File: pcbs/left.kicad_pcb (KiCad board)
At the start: 2 copper layers, 123.5 x 93.6 mm, 27 parts

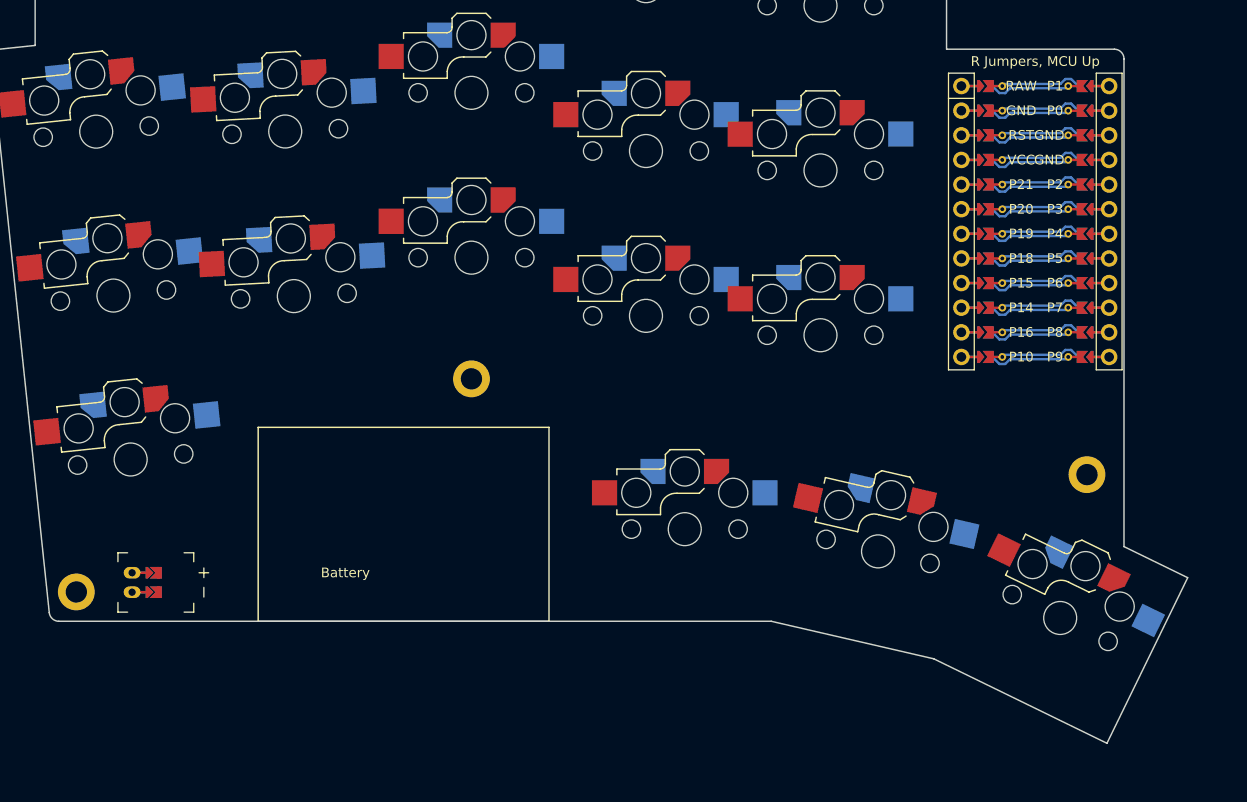
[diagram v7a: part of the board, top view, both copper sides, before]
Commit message: Cut out battery area
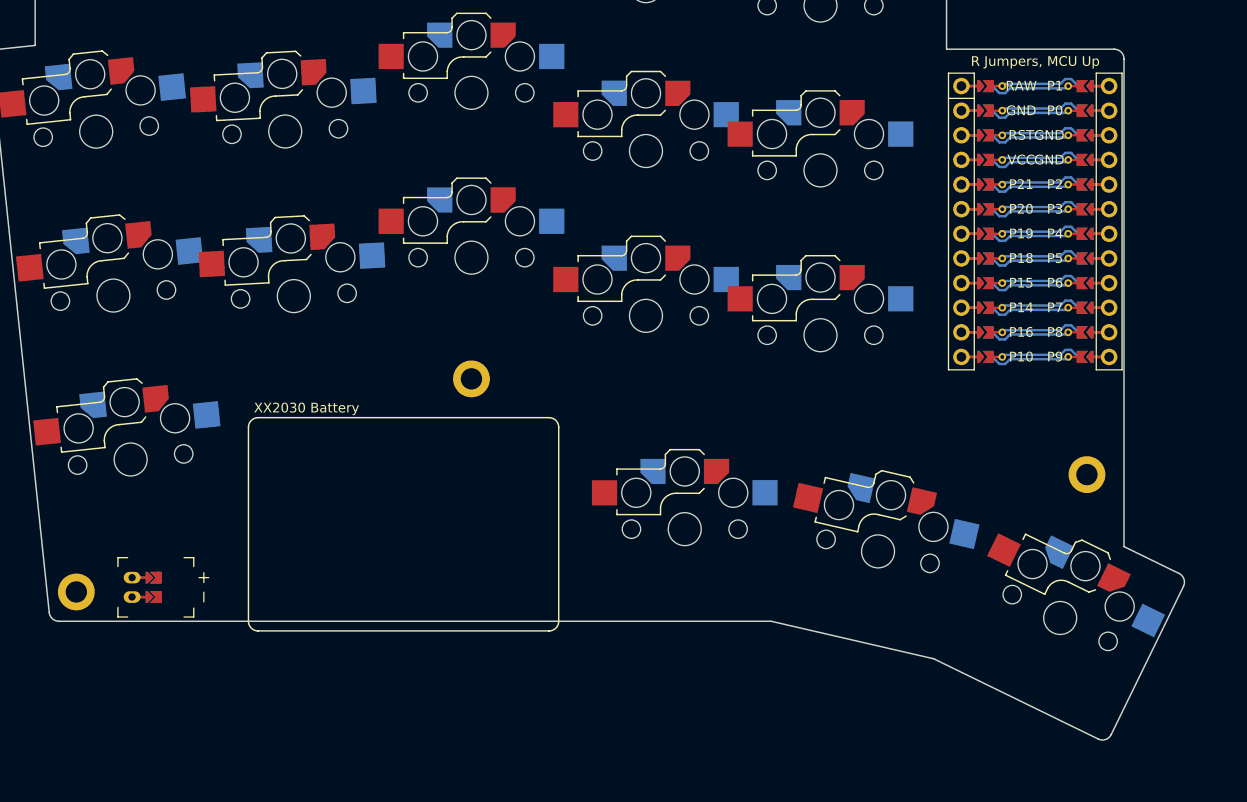
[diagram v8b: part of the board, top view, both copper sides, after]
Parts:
- moved JST1 0.50 mm to (100.1, 113.2)
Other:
- board size 123.5 x 93.6 mm -> 123.2 x 93.2 mm
- board text added: "XX2030 Battery"
- board text removed: "Battery"
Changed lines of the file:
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@@
     (footprint "ceoloide:battery_connector_jst_ph_2"
         (layer "F.Cu")
-        (at 100.1483666 112.68429119999999 90)
+        (at 100.1483666 113.18429119999999 90)
         (property "Reference" "JST1"
             (at 0 4.8 90)
@@
         )
     )
-    (segment (start 101.9483666 113.68429119999999) (end 100.1483666 113.68429119999999) (width 0.25) (layer "F.Cu") (net 53))
-    (segment (start 101.9483666 113.68429119999999) (end 100.1483666 113.68429119999999) (width 0.25) (layer "B.Cu") (net 53))
-    (segment (start 101.9483666 111.68429119999999) (end 100.1483666 111.68429119999999) (width 0.25) (layer "F.Cu") (net 54))
-    (segment (start 101.9483666 111.68429119999999) (end 100.1483666 111.68429119999999) (width 0.25) (layer "B.Cu") (net 54))
-  (gr_text "Battery"
-    (at 122.1483666 111.68429119999999 0)
+    (segment (start 101.9483666 114.18429119999999) (end 100.1483666 114.18429119999999) (width 0.25) (layer "F.Cu") (net 53))
+    (segment (start 101.9483666 114.18429119999999) (end 100.1483666 114.18429119999999) (width 0.25) (layer "B.Cu") (net 53))
+    (segment (start 101.9483666 112.18429119999999) (end 100.1483666 112.18429119999999) (width 0.25) (layer "F.Cu") (net 54))
+    (segment (start 101.9483666 112.18429119999999) (end 100.1483666 112.18429119999999) (width 0.25) (layer "B.Cu") (net 54))
+  (gr_text "XX2030 Battery"
+    (at 118.1483666 94.68429119999999 0)
     (layer "F.SilkS" )
     (effects
@@
         (thickness 0.15)
       )
+    )
+  )
+  (gr_text "XX2030 Battery"
+    (at 118.1483666 94.68429119999999 0)
+    (layer "B.SilkS" )
+    (effects
+      (font
+        (size 1 1)
+        (thickness 0.15)
+      )
+      (justify  mirror)
     )
   )
@@
     (filled_areas_thickness no)
     (fill
-      yes
+      (mode hatch)
       (thermal_gap 0.5)
       (thermal_bridge_width 0.5)
@@
       (island_removal_mode 1)
       (island_area_min 5)
+      (hatch_thickness 1)
+      (hatch_gap 1.5)
+      (hatch_orientation 0)
+      (hatch_border_algorithm hatch_thickness)
+      (hatch_min_hole_area 0.3)
     )
     (polygon
@@
 (gr_line (start 145.1483667 35.68429119999999) (end 125.1483667 35.68429119999999) (layer Edge.Cuts) (stroke (width 0.15) (type default)))
 (gr_line (start 125.1483667 35.68429119999999) (end 125.1483667 39.15278895091144) (layer Edge.Cuts) (stroke (width 0.15) (type default)))
-(gr_line (start 92.5989108808387 116.68429119999999) (end 166.06423773916333 116.68429119999999) (layer Edge.Cuts) (stroke (width 0.15) (type default)))
-(gr_line (start 166.06423773916333 116.68429119999999) (end 182.8265398929574 120.55417358778122) (layer Edge.Cuts) (stroke (width 0.15) (type default)))
-(gr_line (start 182.8265398929574 120.55417358778122) (end 200.6915044 129.2674989) (layer Edge.Cuts) (stroke (width 0.15) (type default)))
-(gr_line (start 200.6915044 129.2674989) (end 209.02055620000002 112.190412) (layer Edge.Cuts) (stroke (width 0.15) (type default)))
-(gr_line (start 209.02055620000002 112.190412) (end 202.4483666 108.9849409801272) (layer Edge.Cuts) (stroke (width 0.15) (type default)))
+(gr_line (start 92.5989108808387 116.68429119999999) (end 165.95030193237426 116.68429119999999) (layer Edge.Cuts) (stroke (width 0.15) (type default)))
+(gr_line (start 166.17525303237426 116.70992109999997) (end 182.71552494111705 120.52854376659285) (layer Edge.Cuts) (stroke (width 0.15) (type default)))
+(gr_line (start 182.92894494111707 120.60411986659285) (end 199.79271042772405 128.82912779290854) (layer Edge.Cuts) (stroke (width 0.15) (type default)))
+(gr_line (start 201.12987552772407 128.3687048929085) (end 208.58218508851954 113.08920597378722) (layer Edge.Cuts) (stroke (width 0.15) (type default)))
+(gr_line (start 208.1217621885195 111.75204087378721) (end 202.4483666 108.98494098012722) (layer Edge.Cuts) (stroke (width 0.15) (type default)))
+(gr_arc (start 166.17525303237426 116.70992109999999) (mid 166.06350513237425 116.69071929999998) (end 165.95030193237426 116.68429119999999) (layer Edge.Cuts) (stroke (width 0.15) (type default)))
+(gr_arc (start 182.92894494111707 120.60411976659283) (mid 182.82438064111705 120.56027236659284) (end 182.71552494111705 120.52854376659283) (layer Edge.Cuts) (stroke (width 0.15) (type default)))
+(gr_arc (start 199.79271042772405 128.82912789290856) (mid 200.55664972772405 128.87585239290857) (end 201.12987562772406 128.36870489290857) (layer Edge.Cuts) (stroke (width 0.15) (type default)))
+(gr_arc (start 208.58218518851953 113.08920597378723) (mid 208.62890968851954 112.32526667378723) (end 208.12176218851954 111.75204077378723) (layer Edge.Cuts) (stroke (width 0.15) (type default)))
 (gr_line (start 184.1483667 57.684291099999996) (end 201.4483666 57.684291099999996) (layer Edge.Cuts) (stroke (width 0.15) (type default)))
-(gr_line (start 202.4483666 108.9849409801272) (end 202.4483666 58.684291099999996) (layer Edge.Cuts) (stroke (width 0.15) (type default)))
+(gr_line (start 202.4483666 108.98494098012722) (end 202.4483666 58.684291099999996) (layer Edge.Cuts) (stroke (width 0.15) (type default)))
 (gr_arc (start 202.4483666 58.684291099999996) (mid 202.1554734 57.9771843) (end 201.4483666 57.684291099999996) (layer Edge.Cuts) (stroke (width 0.15) (type default)))
 (gr_arc (start 91.6043889808387 115.78881969999996) (mid 91.9297802808387 116.42743599999996) (end 92.5989108808387 116.68429119999996) (layer Edge.Cuts) (stroke (width 0.15) (type default)))
@@
 (gr_arc (start 91.1483667 39.18429119999999) (mid 90.44125989999999 39.47718439999999) (end 90.1483667 40.18429119999999) (layer Edge.Cuts) (stroke (width 0.15) (type default)))
 (gr_arc (start 184.1483667 40.18429119999999) (mid 183.8554735 39.47718439999999) (end 183.1483667 39.18429119999999) (layer Edge.Cuts) (stroke (width 0.15) (type default)))
-(gr_line (start 113.1483666 96.68429119999999) (end 113.1483666 116.68429119999999) (layer F.SilkS) (stroke (width 0.15) (type default)))
-(gr_line (start 113.1483666 116.68429119999999) (end 143.1483666 116.68429119999999) (layer F.SilkS) (stroke (width 0.15) (type default)))
-(gr_line (start 143.1483666 116.68429119999999) (end 143.1483666 96.68429119999999) (layer F.SilkS) (stroke (width 0.15) (type default)))
-(gr_line (start 143.1483666 96.68429119999999) (end 113.1483666 96.68429119999999) (layer F.SilkS) (stroke (width 0.15) (type default)))
+(gr_line (start 112.1483666 96.68429119999999) (end 112.1483666 116.68429119999999) (layer F.SilkS) (stroke (width 0.15) (type default)))
+(gr_arc (start 112.1483666 116.68429119999999) (mid 112.4412598 117.391398) (end 113.1483666 117.68429119999999) (layer F.SilkS) (stroke (width 0.15) (type default)))
+(gr_line (start 113.1483666 117.68429119999999) (end 143.1483666 117.68429119999999) (layer F.SilkS) (stroke (width 0.15) (type default)))
+(gr_arc (start 143.1483666 117.68429119999999) (mid 143.8554734 117.391398) (end 144.1483666 116.68429119999999) (layer F.SilkS) (stroke (width 0.15) (type default)))
+(gr_line (start 144.1483666 116.68429119999999) (end 144.1483666 96.68429119999999) (layer F.SilkS) (stroke (width 0.15) (type default)))
+(gr_arc (start 144.1483666 96.68429119999999) (mid 143.8554734 95.97718439999998) (end 143.1483666 95.68429119999999) (layer F.SilkS) (stroke (width 0.15) (type default)))
+(gr_line (start 143.1483666 95.68429119999999) (end 113.1483666 95.68429119999999) (layer F.SilkS) (stroke (width 0.15) (type default)))
+(gr_arc (start 113.1483666 95.68429119999999) (mid 112.4412598 95.97718439999998) (end 112.1483666 96.68429119999999) (layer F.SilkS) (stroke (width 0.15) (type default)))
+(gr_line (start 112.1483666 96.68429119999999) (end 112.1483666 116.68429119999999) (layer B.SilkS) (stroke (width 0.15) (type default)))
+(gr_arc (start 112.1483666 116.68429119999999) (mid 112.4412598 117.391398) (end 113.1483666 117.68429119999999) (layer B.SilkS) (stroke (width 0.15) (type default)))
+(gr_line (start 113.1483666 117.68429119999999) (end 143.1483666 117.68429119999999) (layer B.SilkS) (stroke (width 0.15) (type default)))
+(gr_arc (start 143.1483666 117.68429119999999) (mid 143.8554734 117.391398) (end 144.1483666 116.68429119999999) (layer B.SilkS) (stroke (width 0.15) (type default)))
+(gr_line (start 144.1483666 116.68429119999999) (end 144.1483666 96.68429119999999) (layer B.SilkS) (stroke (width 0.15) (type default)))
+(gr_arc (start 144.1483666 96.68429119999999) (mid 143.8554734 95.97718439999998) (end 143.1483666 95.68429119999999) (layer B.SilkS) (stroke (width 0.15) (type default)))
+(gr_line (start 143.1483666 95.68429119999999) (end 113.1483666 95.68429119999999) (layer B.SilkS) (stroke (width 0.15) (type default)))
+(gr_arc (start 113.1483666 95.68429119999999) (mid 112.4412598 95.97718439999998) (end 112.1483666 96.68429119999999) (layer B.SilkS) (stroke (width 0.15) (type default)))
 )
